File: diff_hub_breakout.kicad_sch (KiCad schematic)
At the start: 4 parts, among them J17 RJ45, U29 MAX3485, U35 MAX3485, U41 MAX3485

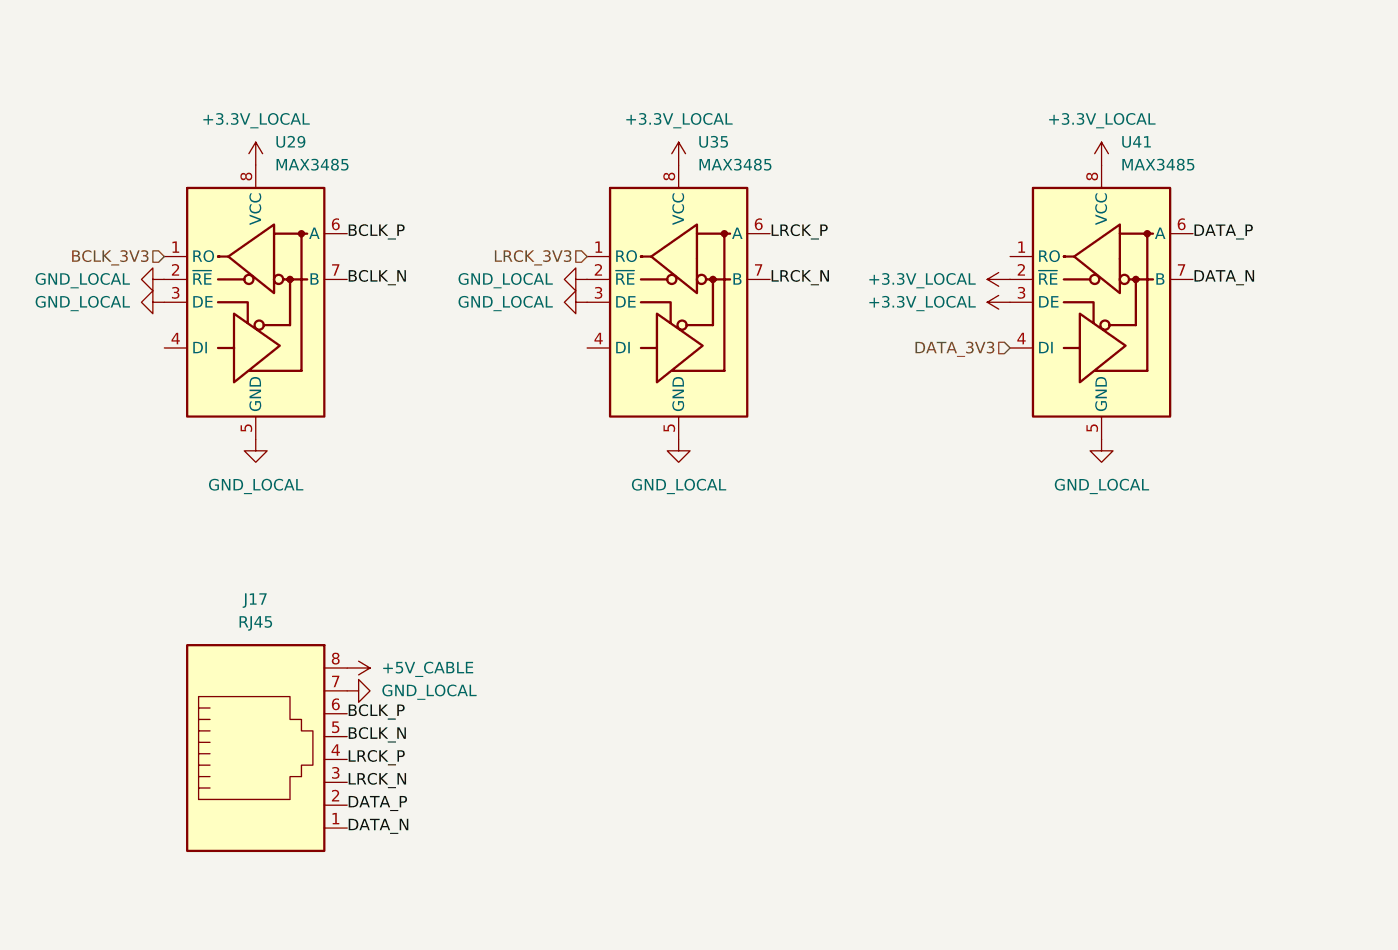
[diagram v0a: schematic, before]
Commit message: Fixed most ERC checks
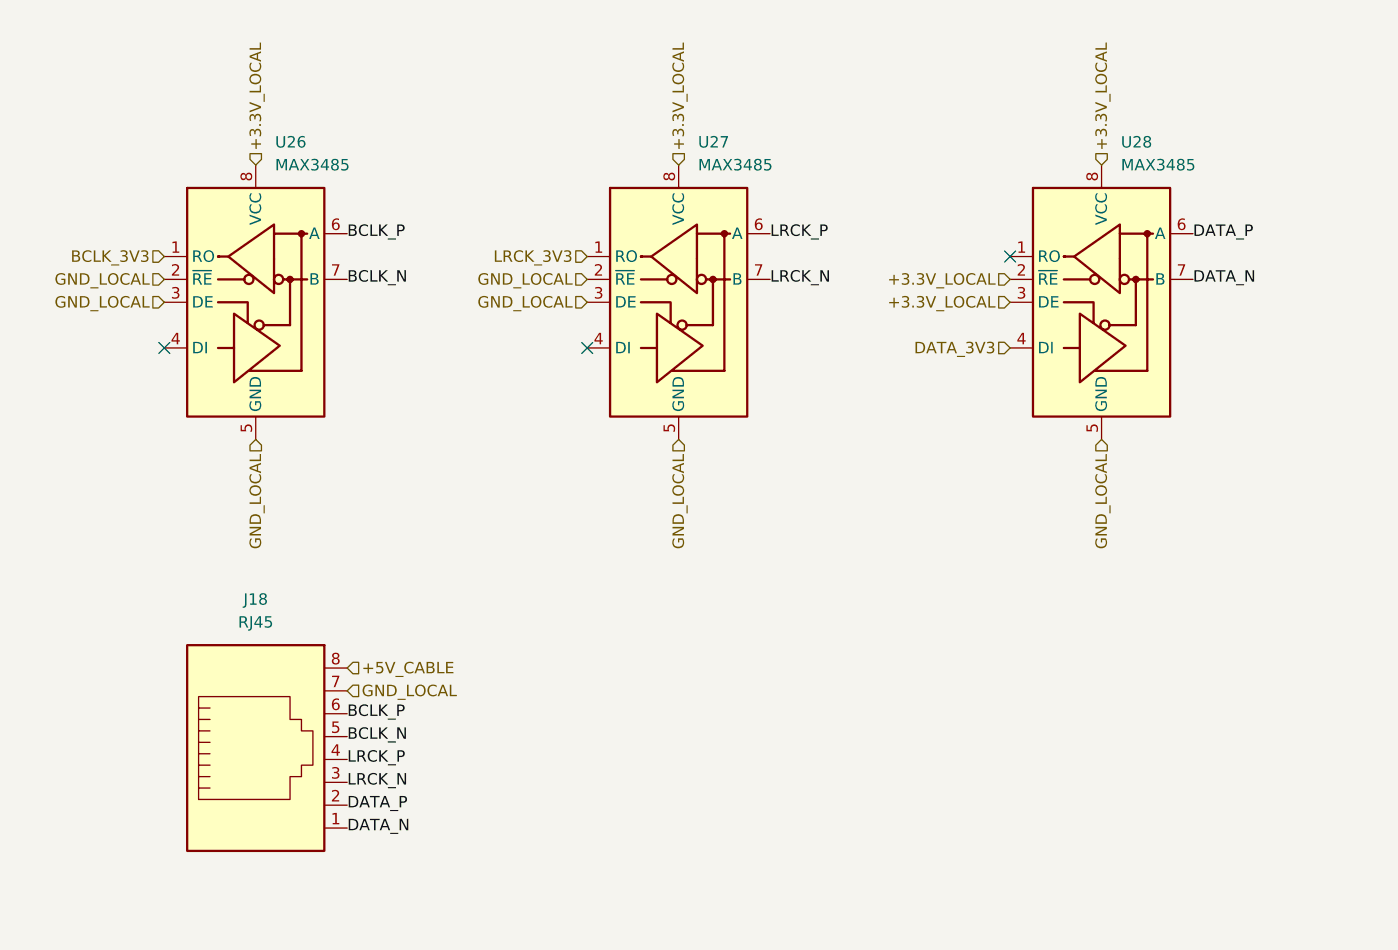
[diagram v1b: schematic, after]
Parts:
- renumbered J17 to J18, U29 to U26, U35 to U27, U41 to U28
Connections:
- no-connect marks 0 -> 3

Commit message: Footprinting done (warnings on schematic side but pcb import works fine)
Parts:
- removed J18: RJ45, symbol Connector:RJ45
- added U59: RJ45, Connector:RJ45-SMD_HC-RJ45-055-4_2, symbol Connector:HC-RJ45-055-4
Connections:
- net +5V_CABLE: now also U59.8
- net BCLK_N: now also U59.5
- net BCLK_P: now also U59.6
- net DATA_N: now also U59.1
- net DATA_P: now also U59.2
- net GND_LOCAL: now also U59.7
- net LRCK_N: now also U59.3
- net LRCK_P: now also U59.4
- new net GND: U59.10, U59.9

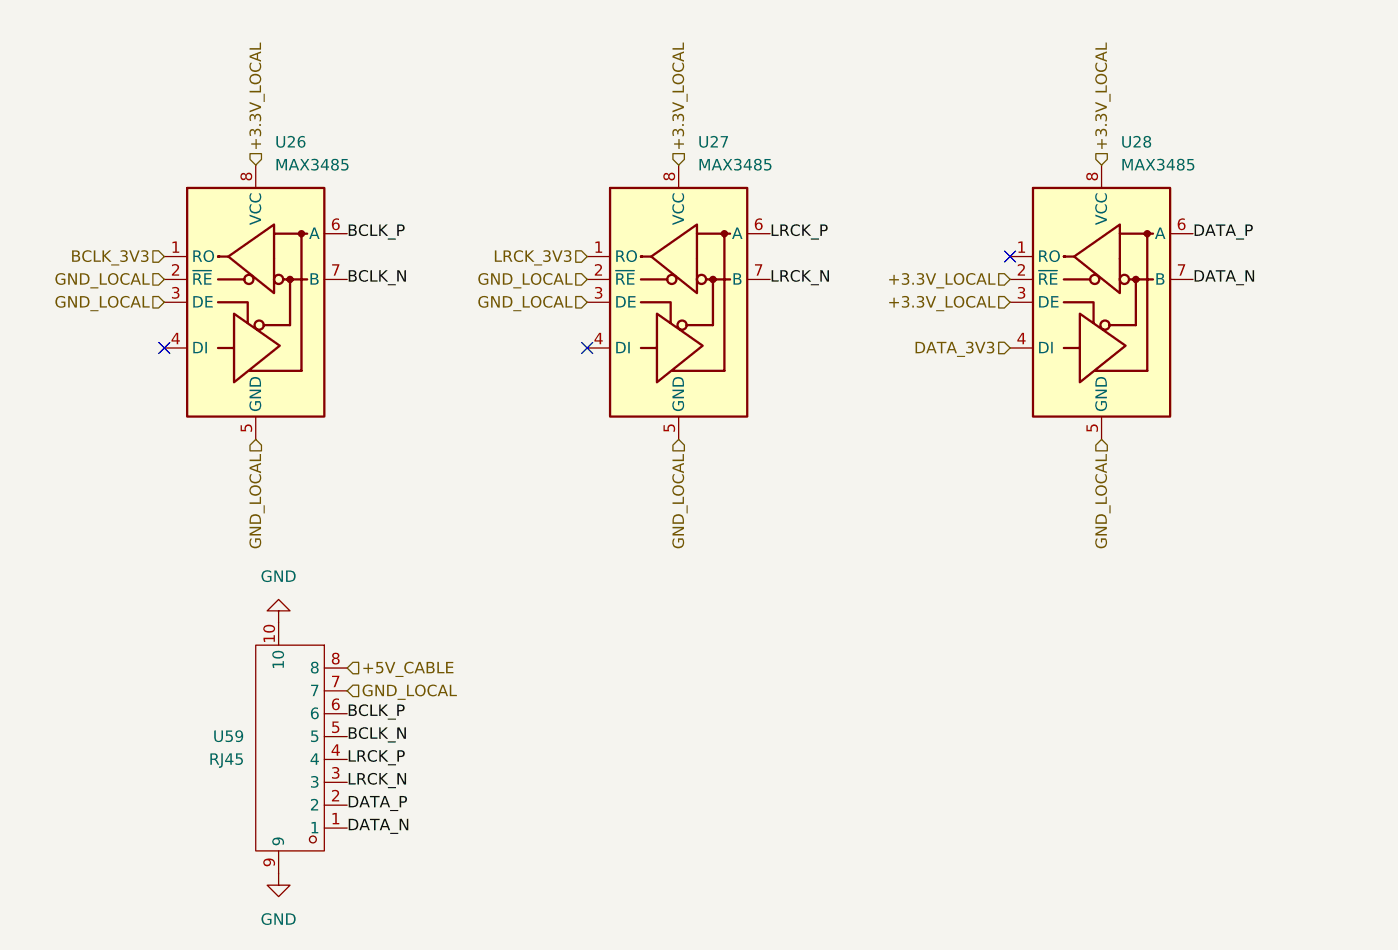
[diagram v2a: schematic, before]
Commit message: Minor schematic changes
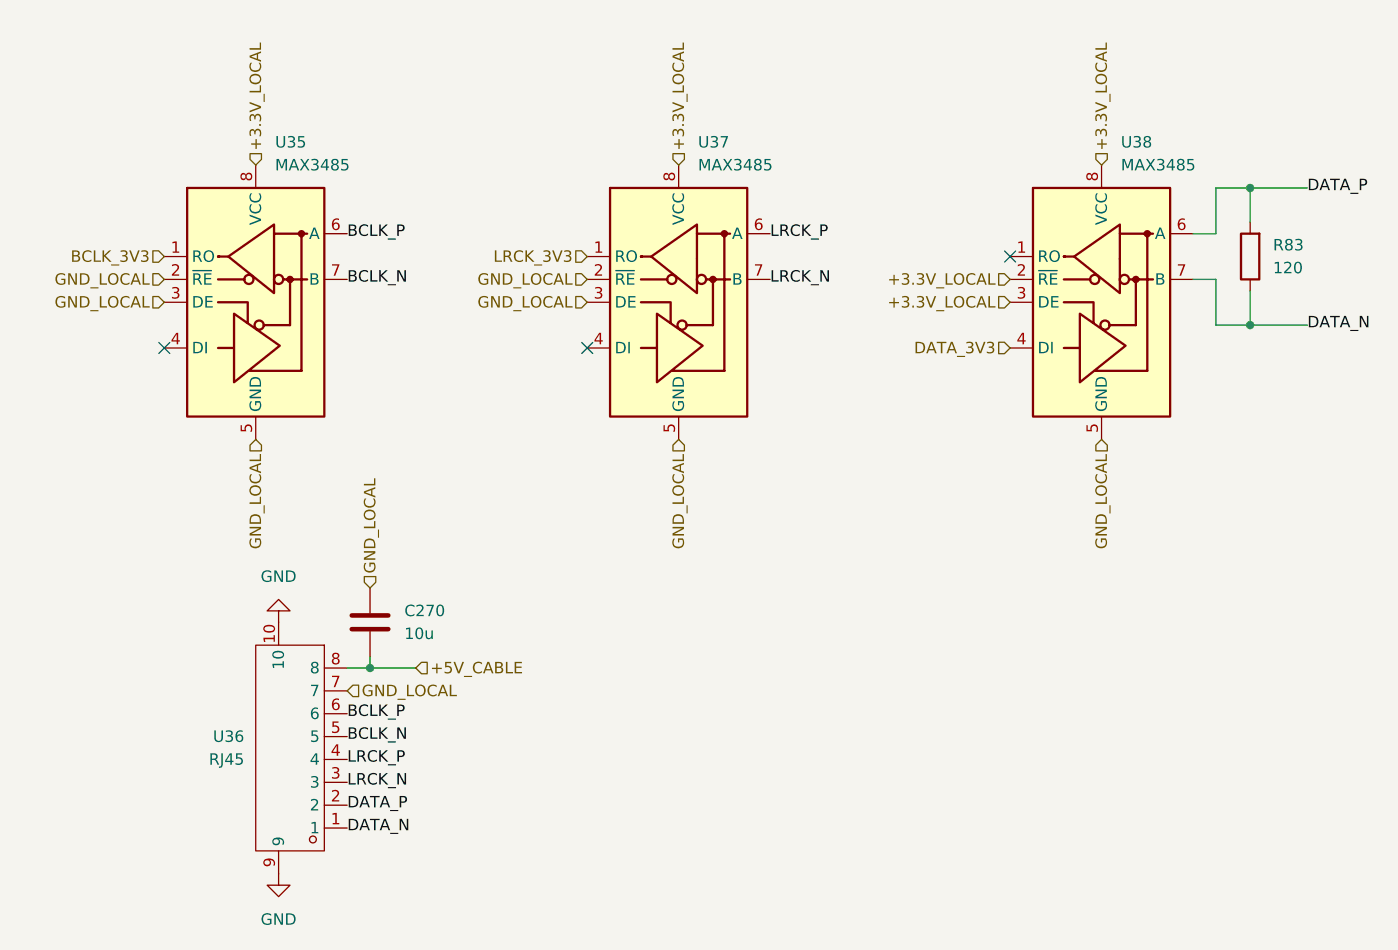
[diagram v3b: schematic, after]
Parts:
- added C270: 10u, Capacitor_SMD:C_0603_1608Metric, symbol Device:C
- added R83: 120, Resistor_SMD:R_0603_1608Metric, symbol Device:R
- renumbered U26 to U35, U59 to U36, U27 to U37, U28 to U38
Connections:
- net +5V_CABLE: now also C270.2
- net DATA_N: now also R83.1
- net DATA_P: now also R83.2
- net GND_LOCAL: now also C270.1
